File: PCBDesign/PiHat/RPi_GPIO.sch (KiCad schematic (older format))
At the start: 12 parts, among them J2 RPi_GPIO, U1 ARDUINO_MICRO_SHIELD

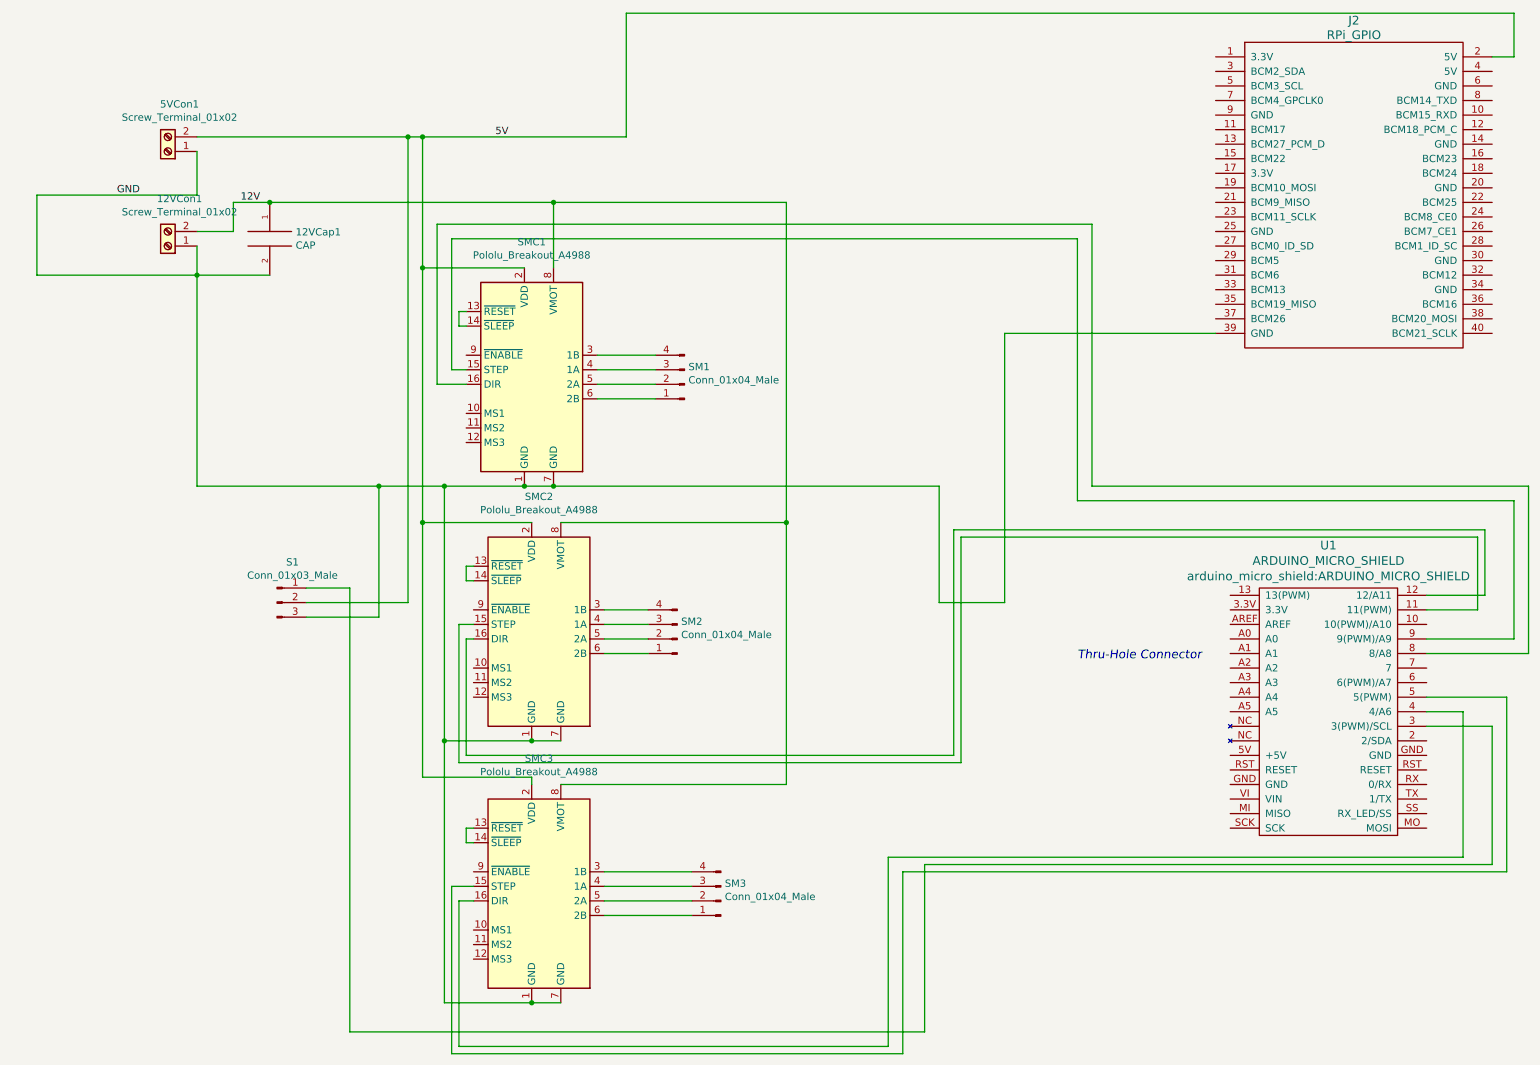
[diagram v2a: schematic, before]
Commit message: Minor fixes, started on traces
Part placement and Nano pins may need to be adjusted. Still missing: MMC and encoder schematic connections, IMU footprint and schematic connections
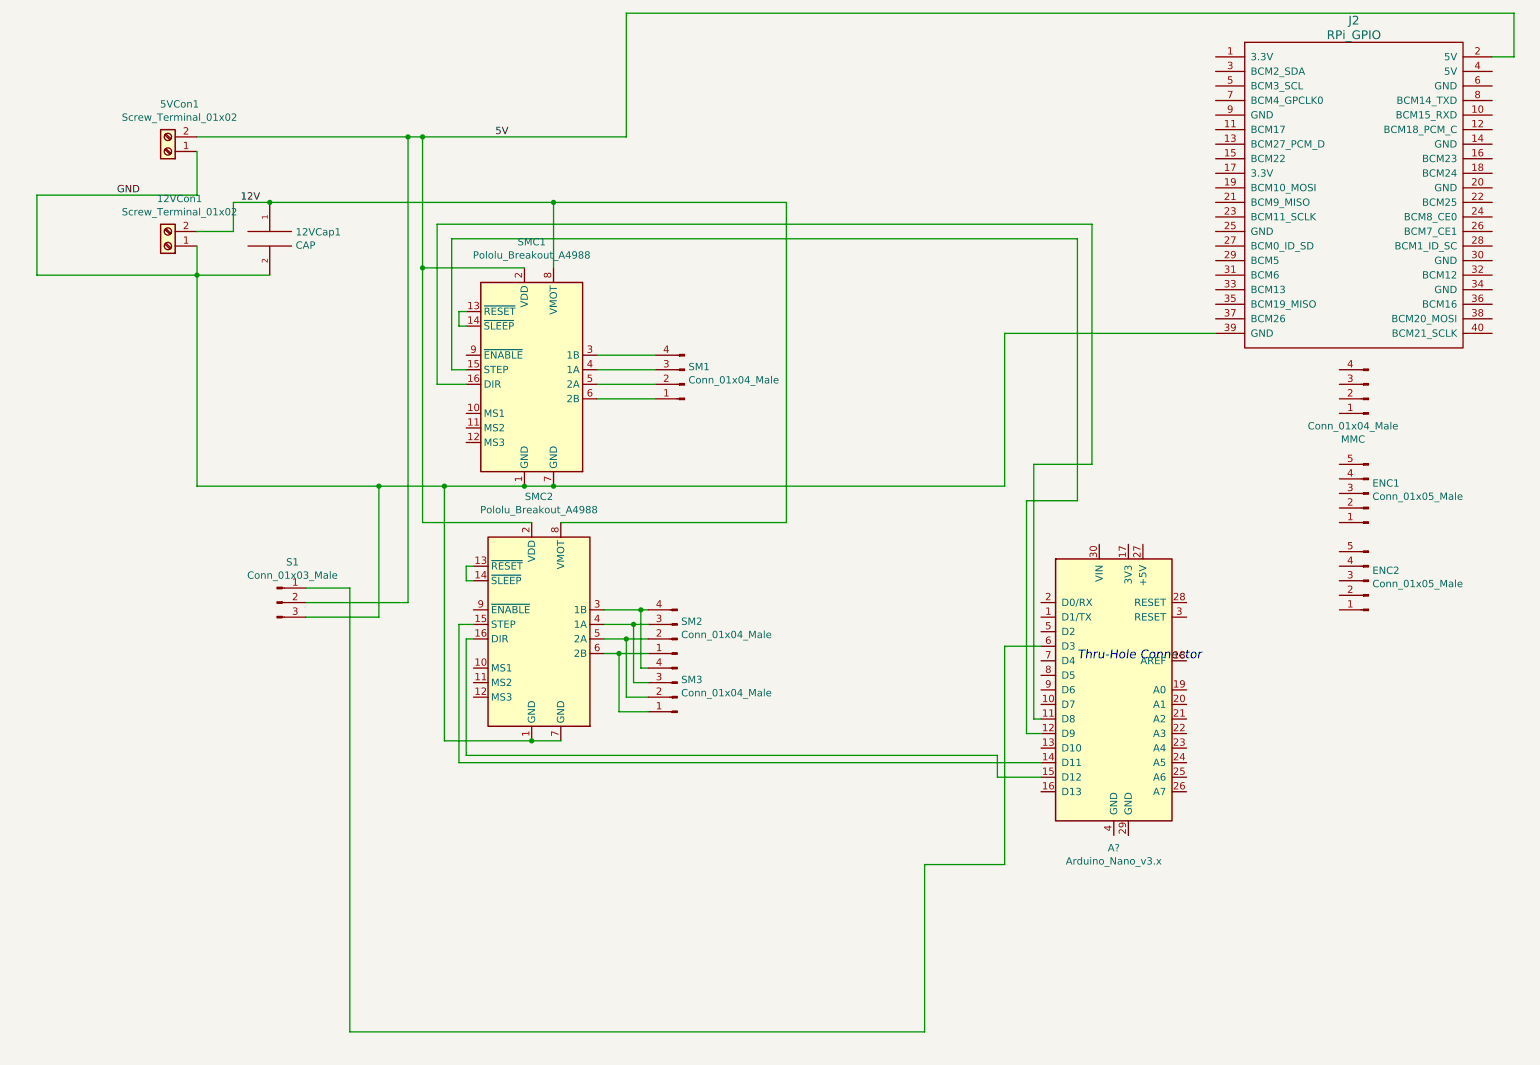
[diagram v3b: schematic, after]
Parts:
- removed SMC3: Pololu_Breakout_A4988, Module:Pololu_Breakout-16_15.2x20.3mm, symbol Driver_Motor:Pololu_Breakout_A4988
- removed U1: ARDUINO_MICRO_SHIELD, arduino_micro_shield:ARDUINO_MICRO_SHIELD, symbol arduino_micro_shield:ARDUINO_MICRO_SHIELD
- added A?: Arduino_Nano_v3.x, Module:Arduino_Nano, symbol MCU_Module:Arduino_Nano_v3.x
- added ENC1, ENC2: Conn_01x05_Male, Connector_PinHeader_2.54mm:PinHeader_1x05_P2.54mm_Vertical, symbol Connector:Conn_01x05_Male
- added MMC: Conn_01x04_Male, Connector:NS-Tech_Grove_1x04_P2mm_Vertical, symbol Connector:Conn_01x04_Male
- 12VCap1: footprint Capacitor_THT:CP_Axial_L10.0mm_D4.5mm_P15.00mm_Horizontal -> Capacitor_THT:C_Rect_L9.0mm_W6.7mm_P7.50mm_MKT
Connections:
- net at SMC1.15 (STEP): now also A?.12 (D9)
- net at SMC1.16 (DIR): now also A?.11 (D8)
- net at SMC2.15 (STEP): now also A?.14 (D11)
- net at SMC2.16 (DIR): now also A?.15 (D12)
- net at SM2.4 (Pin_4), SMC2.3 (1B): now also SM3.4 (Pin_4)
- net at SM2.3 (Pin_3), SMC2.4 (1A): now also SM3.3 (Pin_3)
- net at SM2.2 (Pin_2), SMC2.5 (2A): now also SM3.2 (Pin_2)
- net at SM2.1 (Pin_1), SMC2.6 (2B): now also SM3.1 (Pin_1)
- net at S1.1 (Pin_1): now also A?.6 (D3)
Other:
- moved on the sheet: SM3
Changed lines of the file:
@@
 EESchema Schematic File Version 4
-LIBS:RPi_Hat-cache
+LIBS:RPi_GPIO-cache
 EELAYER 26 0
 EELAYER END
 $Descr A4 11693 8268
 encoding utf-8
-Sheet 1 2
+Sheet 1 1
 Title ""
 Date ""
@@
 $EndComp
 $Comp
-L Driver_Motor:Pololu_Breakout_A4988 SMC3
-U 1 1 5C782A2D
-P 4050 6550
-F 0 "SMC3" H 4100 7428 50  0000 C CNN
-F 1 "Pololu_Breakout_A4988" H 4100 7337 50  0000 C CNN
-F 2 "Module:Pololu_Breakout-16_15.2x20.3mm" H 4325 5800 50  0001 L CNN
-F 3 "https://www.pololu.com/product/2980/pictures" H 4150 6250 50  0001 C CNN
-	1    4050 6550
-	1    0    0    -1
-$EndComp
-$Comp
-L arduino_micro_shield:ARDUINO_MICRO_SHIELD U1
-U 1 1 5C782D02
-P 10000 6200
-F 0 "U1" V 11993 6675 60  0000 C CNN
-F 1 "ARDUINO_MICRO_SHIELD" V 11887 6675 60  0000 C CNN
-F 2 "arduino_micro_shield:ARDUINO_MICRO_SHIELD" V 11781 6675 60  0000 C CNN
-F 3 "" H 10400 6150 60  0000 C CNN
-	1    10000 6200
-	0    -1   -1   0
-$EndComp
-$Comp
 L pspice:CAP 12VCap1
 U 1 1 5C782DDC
@@
 F 0 "12VCap1" H 2428 2146 50  0000 L CNN
 F 1 "CAP" H 2428 2055 50  0000 L CNN
-F 2 "Capacitor_THT:CP_Axial_L10.0mm_D4.5mm_P15.00mm_Horizontal" H 2250 2100 50  0001 C CNN
+F 2 "Capacitor_THT:C_Rect_L9.0mm_W6.7mm_P7.50mm_MKT" H 2250 2100 50  0001 C CNN
 F 3 "~" H 2250 2100 50  0001 C CNN
 	1    2250 2100
@@
 Wire Wire Line
 	3450 3800 3450 5550
-Wire Wire Line
-	3450 5550 4050 5550
 Connection ~ 3450 3800
 Wire Wire Line
 	3450 3800 4000 3800
-Wire Wire Line
-	4250 5550 4050 5550
-Connection ~ 4050 5550
-Wire Wire Line
-	3450 5550 3450 7350
-Wire Wire Line
-	3450 7350 4050 7350
-Connection ~ 3450 5550
-Wire Wire Line
-	4250 7350 4050 7350
-Connection ~ 4050 7350
-Wire Wire Line
-	4200 3800 6850 3800
-Wire Wire Line
-	6850 3800 6850 4600
-Wire Wire Line
-	6850 4600 7300 4600
 Connection ~ 4200 3800
 Wire Wire Line
@@
 5V
 Wire Wire Line
-	7300 4600 7300 2750
-Wire Wire Line
 	7300 2750 8750 2750
 Wire Wire Line
-	4850 4950 4550 4950
-Wire Wire Line
-	4850 4850 4550 4850
-Wire Wire Line
-	4850 4750 4550 4750
-Wire Wire Line
-	4850 4650 4550 4650
+	4850 4950 4650 4950
 Wire Wire Line
 	4900 3200 4500 3200
@@
 	6750 7550 6750 6400
 Wire Wire Line
-	6750 6400 10650 6400
-Wire Wire Line
-	10650 6400 10650 5450
-Wire Wire Line
-	10650 5450 10200 5450
-Wire Wire Line
 	4050 4050 3300 4050
 Wire Wire Line
@@
 	3300 1400 4700 1400
 Wire Wire Line
-	3300 4050 3300 5800
-Wire Wire Line
-	3300 5800 4050 5800
-Wire Wire Line
-	4050 5800 4050 5850
-Connection ~ 3300 4050
-Wire Wire Line
 	3300 2300 4000 2300
 Connection ~ 3300 2300
@@
 Connection ~ 4200 1850
 Wire Wire Line
-	5800 4050 5800 5850
-Wire Wire Line
-	5800 5850 4250 5850
-Connection ~ 5800 4050
-Wire Wire Line
-	3650 6150 3600 6150
-Wire Wire Line
-	3600 6150 3600 6250
-Wire Wire Line
-	3600 6250 3650 6250
-Wire Wire Line
 	3650 4350 3600 4350
 Wire Wire Line
@@
 	3400 2000 7900 2000
 Wire Wire Line
-	7900 2000 7900 3800
-Wire Wire Line
-	7900 3800 10900 3800
-Wire Wire Line
-	10900 3800 10900 4950
-Wire Wire Line
-	10900 4950 10200 4950
+	7900 2000 7900 3650
 Wire Wire Line
 	3600 3000 3500 3000
@@
 	7800 2100 7800 3900
 Wire Wire Line
-	7800 3900 10800 3900
-Wire Wire Line
-	10800 3900 10800 4850
-Wire Wire Line
-	10800 4850 10200 4850
-Wire Wire Line
-	10200 4550 10600 4550
-Wire Wire Line
-	10600 4550 10600 4100
-Wire Wire Line
-	10600 4100 6950 4100
-Wire Wire Line
-	6950 4100 6950 5650
-Wire Wire Line
-	6950 5650 3600 5650
-Wire Wire Line
 	3600 5650 3600 4850
 Wire Wire Line
@@
 Wire Wire Line
 	3550 4750 3550 5700
-Wire Wire Line
-	3550 5700 7000 5700
-Wire Wire Line
-	7000 5700 7000 4150
-Wire Wire Line
-	7000 4150 10550 4150
-Wire Wire Line
-	10550 4150 10550 4650
-Wire Wire Line
-	10550 4650 10200 4650
-Wire Wire Line
-	3650 6650 3550 6650
-Wire Wire Line
-	3550 6650 3550 7650
-Wire Wire Line
-	3550 7650 6500 7650
-Wire Wire Line
-	6500 7650 6500 6350
-Wire Wire Line
-	6500 6350 10450 6350
-Wire Wire Line
-	10450 6350 10450 5350
-Wire Wire Line
-	10450 5350 10200 5350
-Wire Wire Line
-	3650 6550 3500 6550
-Wire Wire Line
-	3500 6550 3500 7700
-Wire Wire Line
-	3500 7700 6600 7700
-Wire Wire Line
-	6600 7700 6600 6450
-Wire Wire Line
-	6600 6450 10750 6450
-Wire Wire Line
-	10750 6450 10750 5250
-Wire Wire Line
-	10750 5250 10200 5250
 $Comp
 L Connector:Conn_01x04_Male SM3
 U 1 1 5C7AD885
-P 5350 6650
-F 0 "SM3" H 5323 6530 50  0000 R CNN
-F 1 "Conn_01x04_Male" H 5323 6621 50  0000 R CNN
-F 2 "Connector_PinHeader_2.54mm:PinHeader_1x04_P2.54mm_Vertical" H 5350 6650 50  0001 C CNN
-F 3 "~" H 5350 6650 50  0001 C CNN
-	1    5350 6650
-	-1   0    0    1
-$EndComp
-Wire Wire Line
-	4550 6450 5150 6450
-Wire Wire Line
-	4550 6550 5150 6550
-Wire Wire Line
-	4550 6650 5150 6650
-Wire Wire Line
-	4550 6750 5150 6750
+P 5050 5250
+F 0 "SM3" H 5023 5130 50  0000 R CNN
+F 1 "Conn_01x04_Male" H 5023 5221 50  0000 R CNN
+F 2 "Connector_PinHeader_2.54mm:PinHeader_1x04_P2.54mm_Vertical" H 5050 5250 50  0001 C CNN
+F 3 "~" H 5050 5250 50  0001 C CNN
+	1    5050 5250
+	-1   0    0    1
+$EndComp
+Wire Wire Line
+	4550 4850 4700 4850
+Wire Wire Line
+	3450 5550 4050 5550
+Wire Wire Line
+	4250 5550 4050 5550
+Connection ~ 4050 5550
+Wire Wire Line
+	4550 4650 4800 4650
+Wire Wire Line
+	4550 4750 4750 4750
+Wire Wire Line
+	4800 4650 4800 5050
+Wire Wire Line
+	4800 5050 4850 5050
+Connection ~ 4800 4650
+Wire Wire Line
+	4800 4650 4850 4650
+Wire Wire Line
+	4750 4750 4750 5150
+Wire Wire Line
+	4750 5150 4850 5150
+Connection ~ 4750 4750
+Wire Wire Line
+	4750 4750 4850 4750
+Wire Wire Line
+	4700 4850 4700 5250
+Wire Wire Line
+	4700 5250 4850 5250
+Connection ~ 4700 4850
+Wire Wire Line
+	4700 4850 4850 4850
+Wire Wire Line
+	4650 4950 4650 5350
+Wire Wire Line
+	4650 5350 4850 5350
+Connection ~ 4650 4950
+Wire Wire Line
+	4650 4950 4550 4950
+$Comp
+L MCU_Module:Arduino_Nano_v3.x A?
+U 1 1 5C80A084
+P 8050 5200
+F 0 "A?" H 8050 4114 50  0000 C CNN
+F 1 "Arduino_Nano_v3.x" H 8050 4023 50  0000 C CNN
+F 2 "Module:Arduino_Nano" H 8200 4250 50  0001 L CNN
+F 3 "http://www.mouser.com/pdfdocs/Gravitech_Arduino_Nano3_0.pdf" H 8050 4200 50  0001 C CNN
+	1    8050 5200
+	1    0    0    -1
+$EndComp
+Wire Wire Line
+	6750 6400 7300 6400
+Wire Wire Line
+	7300 6400 7300 4900
+Wire Wire Line
+	7300 4900 7550 4900
+Wire Wire Line
+	3550 5700 7550 5700
+Wire Wire Line
+	7250 5650 7250 5800
+Wire Wire Line
+	7250 5800 7550 5800
+Wire Wire Line
+	3600 5650 7250 5650
+Wire Wire Line
+	7800 3900 7450 3900
+Wire Wire Line
+	7450 3900 7450 5500
+Wire Wire Line
+	7450 5500 7550 5500
+Wire Wire Line
+	7900 3650 7500 3650
+Wire Wire Line
+	7500 3650 7500 5400
+Wire Wire Line
+	7500 5400 7550 5400
+Wire Wire Line
+	7300 2750 7300 3800
+Wire Wire Line
+	4200 3800 7300 3800
+$Comp
+L Connector:Conn_01x04_Male MMC
+U 1 1 5C83F9B6
+P 9800 3200
+F 0 "MMC" H 9906 3478 50  0000 C CNN
+F 1 "Conn_01x04_Male" H 9906 3387 50  0000 C CNN
+F 2 "Connector:NS-Tech_Grove_1x04_P2mm_Vertical" H 9800 3200 50  0001 C CNN
+F 3 "~" H 9800 3200 50  0001 C CNN
+	1    9800 3200
+	-1   0    0    1
+$EndComp
+$Comp
+L Connector:Conn_01x05_Male ENC1
+U 1 1 5C84907A
+P 9800 3850
+F 0 "ENC1" H 9773 3780 50  0000 R CNN
+F 1 "Conn_01x05_Male" H 9773 3871 50  0000 R CNN
+F 2 "Connector_PinHeader_2.54mm:PinHeader_1x05_P2.54mm_Vertical" H 9800 3850 50  0001 C CNN
+F 3 "~" H 9800 3850 50  0001 C CNN
+	1    9800 3850
+	-1   0    0    1
+$EndComp
+$Comp
+L Connector:Conn_01x05_Male ENC2
+U 1 1 5C8526DD
+P 9800 4450
+F 0 "ENC2" H 9773 4380 50  0000 R CNN
+F 1 "Conn_01x05_Male" H 9773 4471 50  0000 R CNN
+F 2 "Connector_PinHeader_2.54mm:PinHeader_1x05_P2.54mm_Vertical" H 9800 4450 50  0001 C CNN
+F 3 "~" H 9800 4450 50  0001 C CNN
+	1    9800 4450
+	-1   0    0    1
+$EndComp
 $EndSCHEMATC
